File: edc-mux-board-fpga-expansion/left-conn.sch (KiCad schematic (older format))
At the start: 68 parts

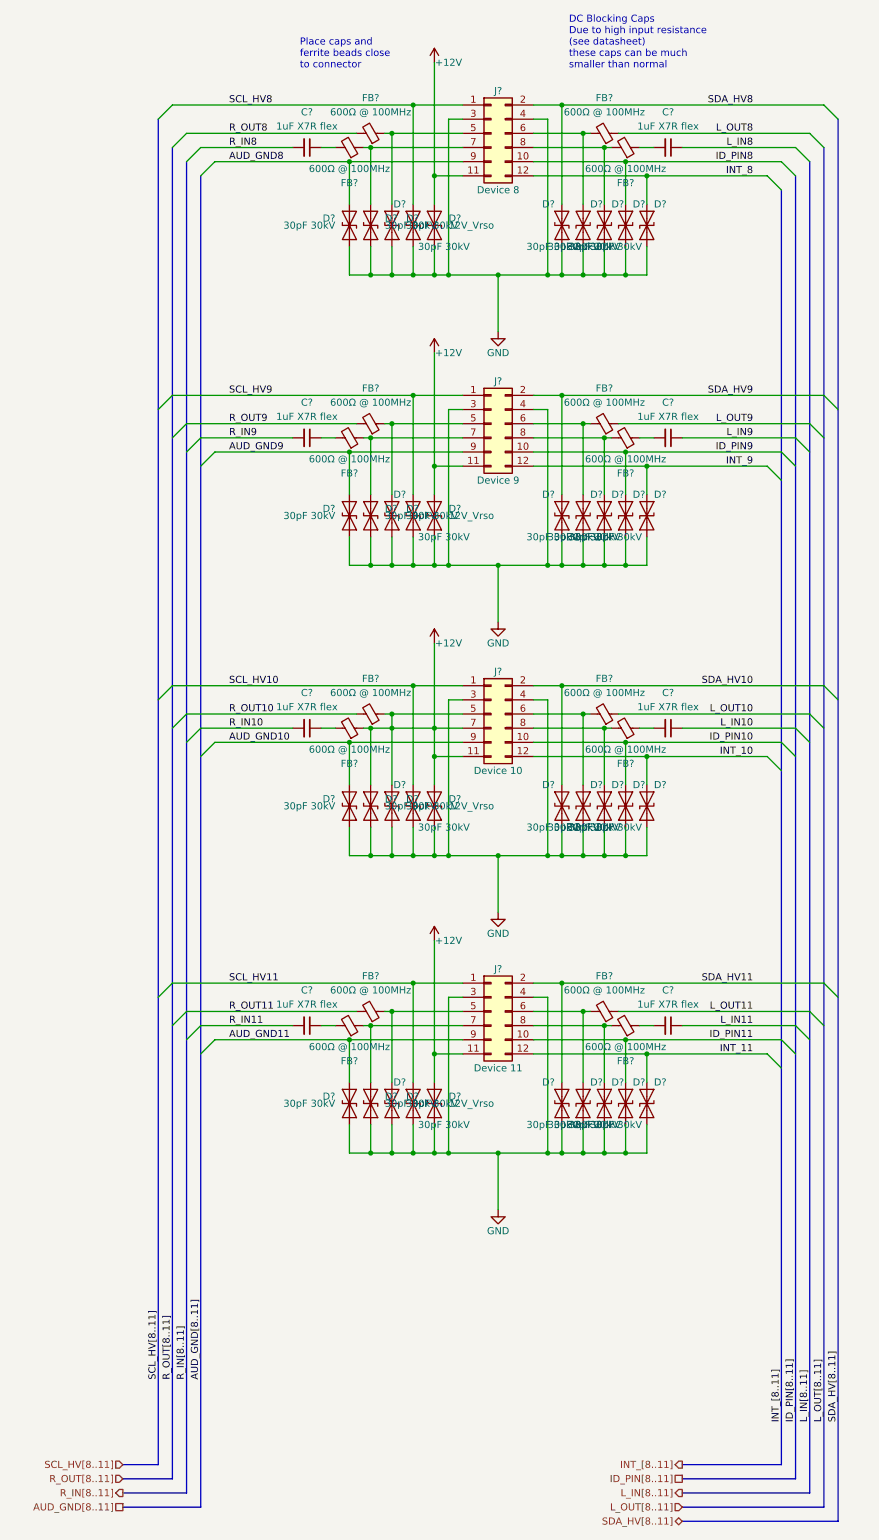
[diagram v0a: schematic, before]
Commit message: Annotating modified components
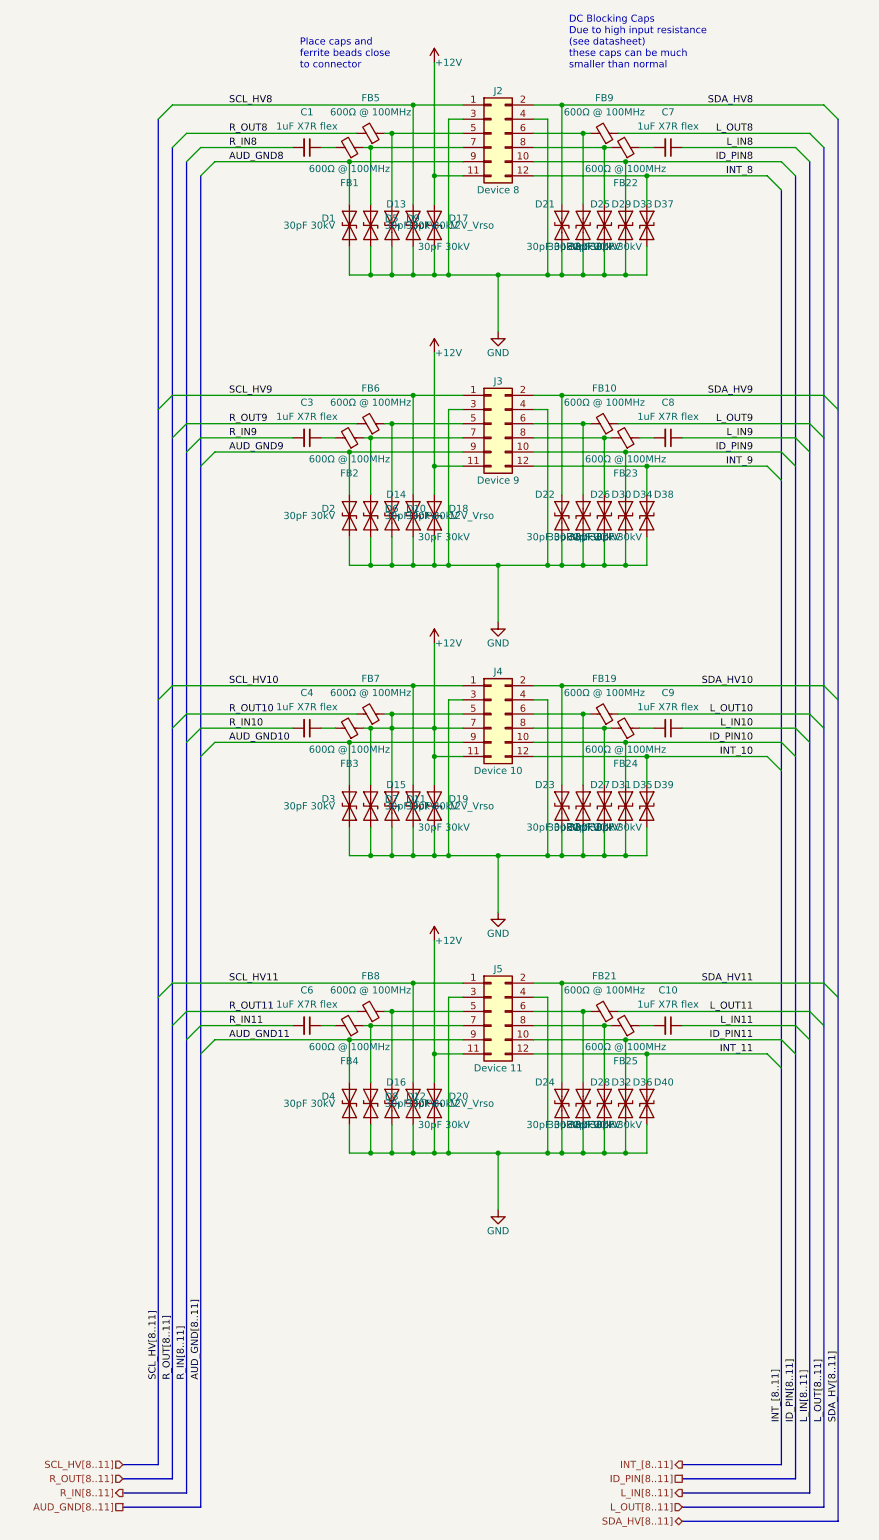
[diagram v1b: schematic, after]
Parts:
- gave numbers to parts that had none: 68

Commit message: Reannotating entire schematic
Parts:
- renumbered C1 to C154, C3 to C155, C4 to C156, C6 to C157, C7 to C158, C8 to C159, C9 to C160, C10 to C161, FB1 to FB10, FB2 to FB11, FB3 to FB12, FB4 to FB13, FB5 to FB14, FB6 to FB15, FB7 to FB16, FB8 to FB17, FB9 to FB18, FB10 to FB19, FB19 to FB20
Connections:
- net +12V: no longer D11.1 (A1), D7.1 (A1), FB12.1, FB16.1, J4.5 (Pin_5), J4.7 (Pin_7)
- new net: D11.1 (A1), FB16.1, J4.5 (Pin_5)
- new net: D7.1 (A1), FB12.1, J4.7 (Pin_7)

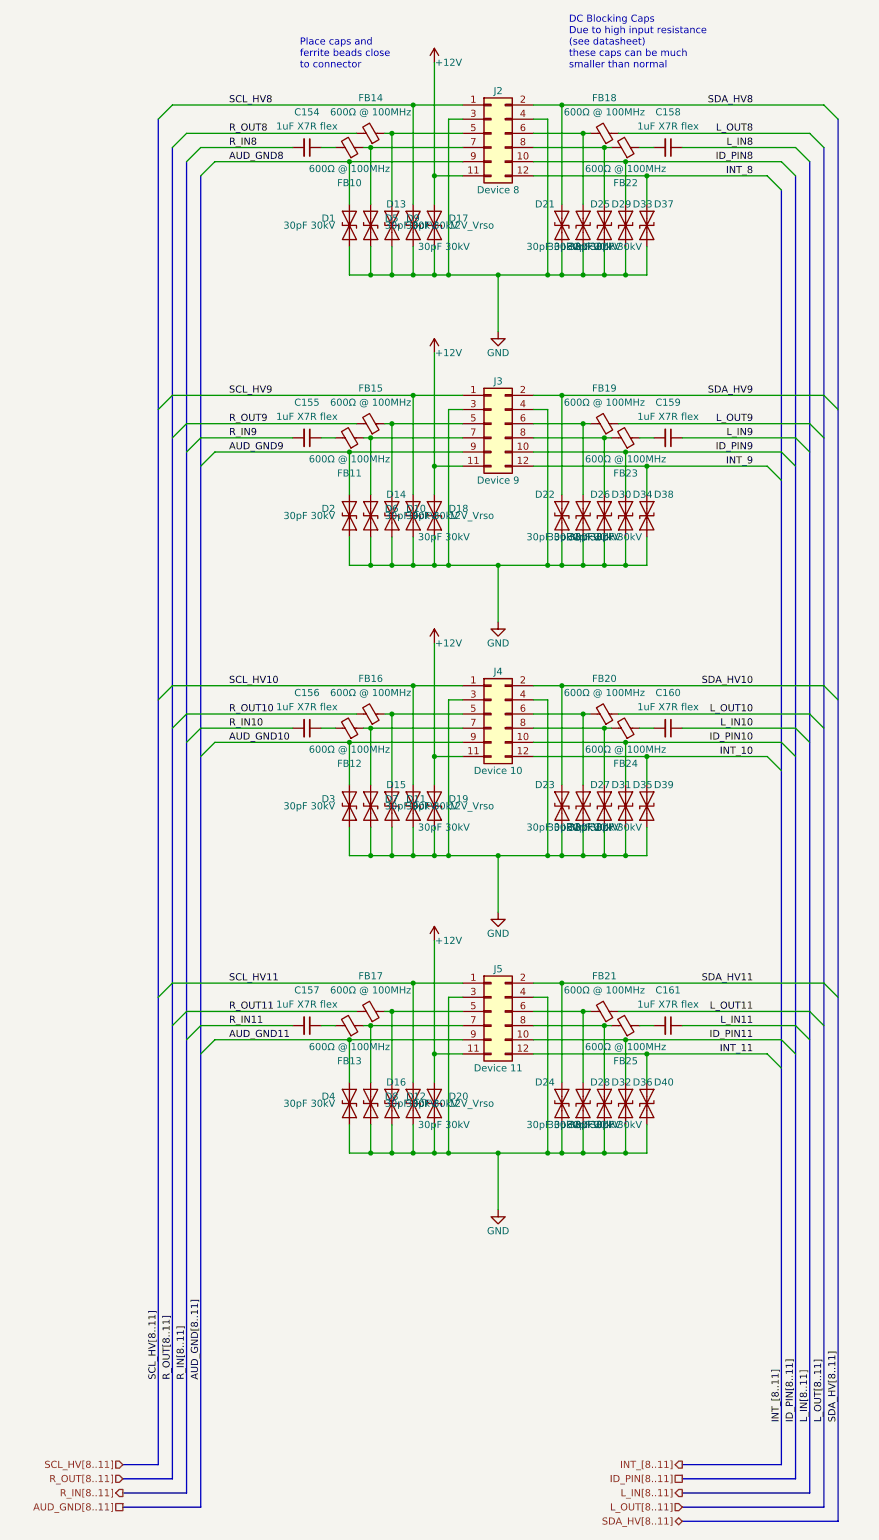
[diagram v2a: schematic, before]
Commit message: Revert "Reannotating entire schematic"
This reverts commit 97c3612cc2b740b2bdf3282f0b448b6cc86bc5bb.
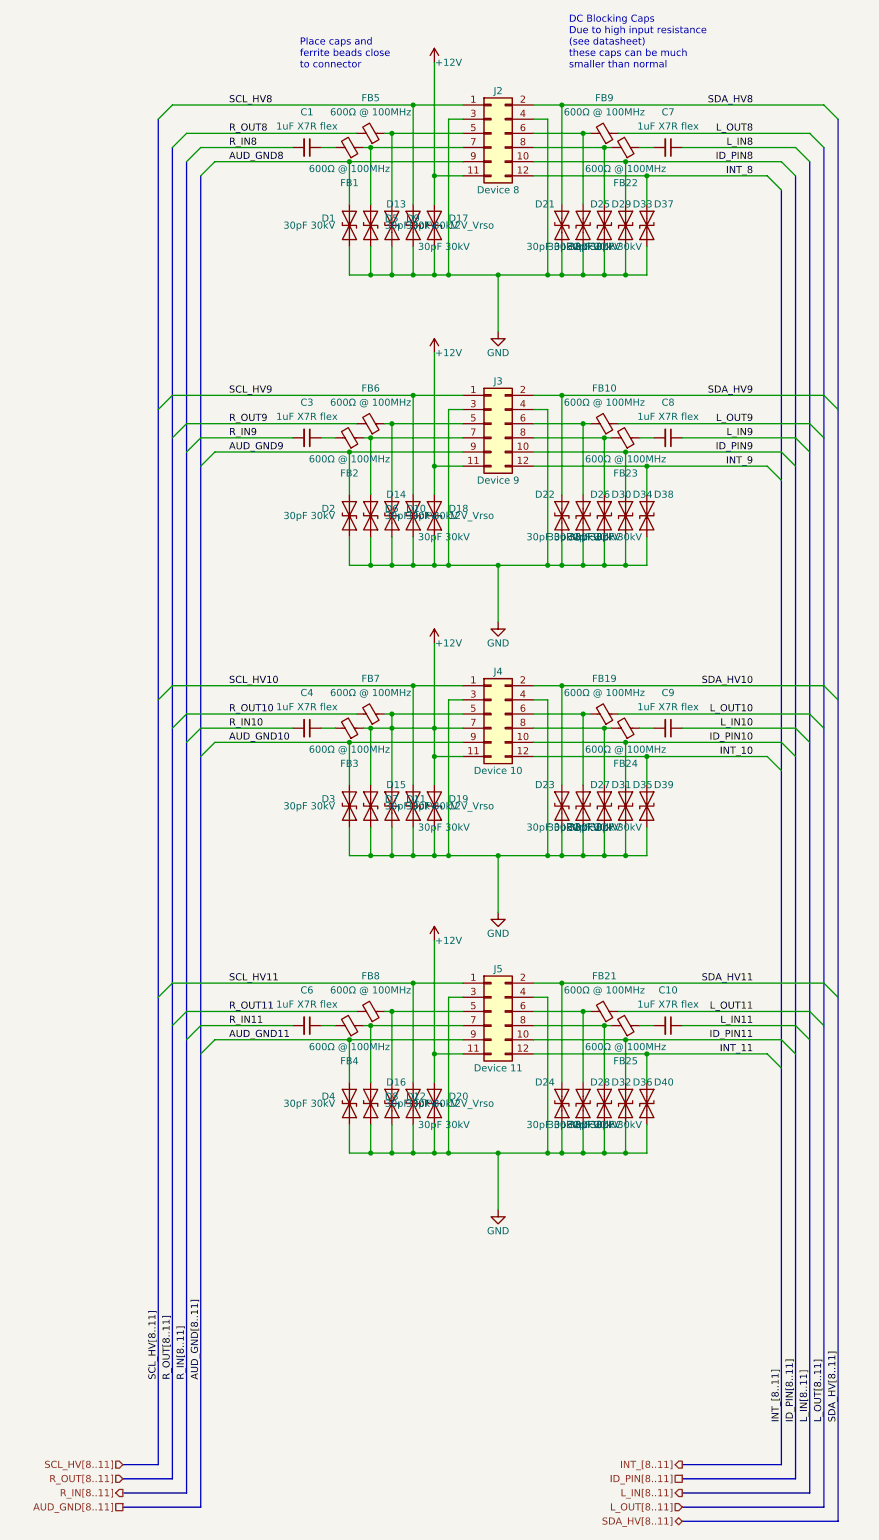
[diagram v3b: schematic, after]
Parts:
- renumbered C154 to C1, C161 to C10, C155 to C3, C156 to C4, C157 to C6, C158 to C7, C159 to C8, C160 to C9, FB10 to FB1, FB19 to FB10, FB20 to FB19, FB11 to FB2, FB12 to FB3, FB13 to FB4, FB14 to FB5, FB15 to FB6, FB16 to FB7, FB17 to FB8, FB18 to FB9
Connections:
- net +12V: now also D11.1 (A1), D7.1 (A1), FB3.1, FB7.1, J4.5 (Pin_5), J4.7 (Pin_7)

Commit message: Figured out what option to use to reannotate the schematic properly
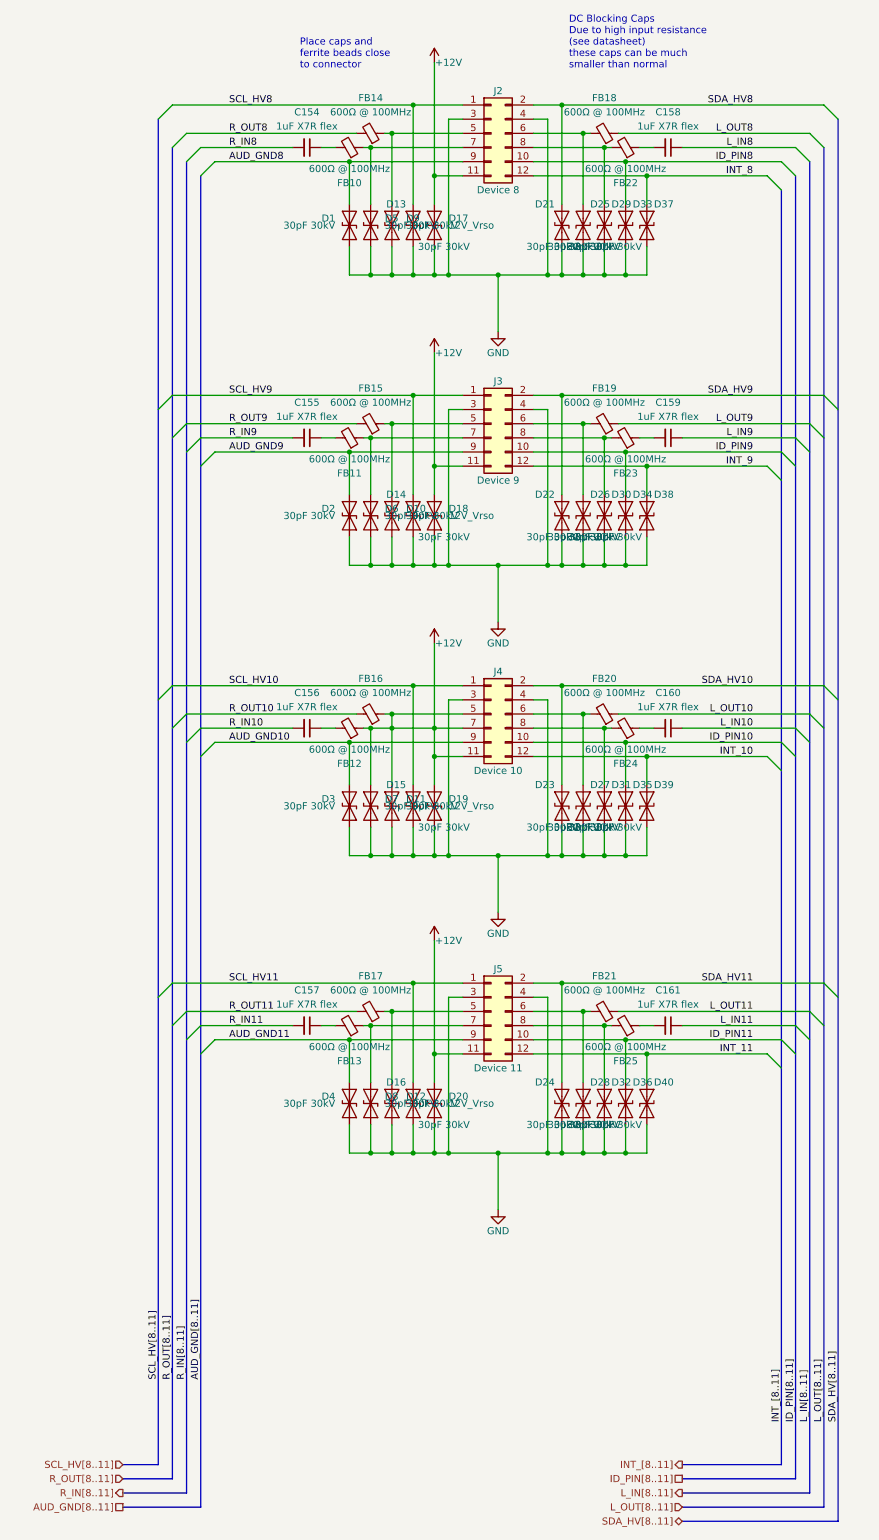
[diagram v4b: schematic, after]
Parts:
- renumbered C1 to C154, C3 to C155, C4 to C156, C6 to C157, C7 to C158, C8 to C159, C9 to C160, C10 to C161, FB1 to FB10, FB2 to FB11, FB3 to FB12, FB4 to FB13, FB5 to FB14, FB6 to FB15, FB7 to FB16, FB8 to FB17, FB9 to FB18, FB10 to FB19, FB19 to FB20

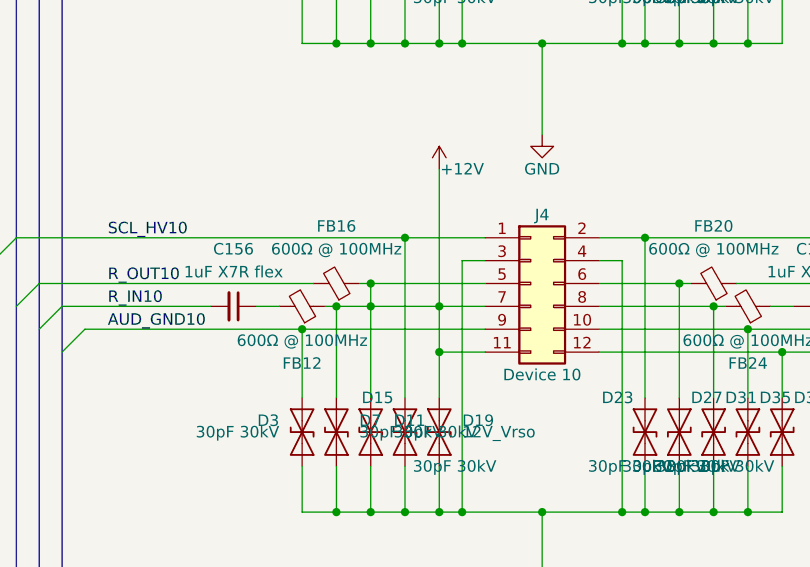
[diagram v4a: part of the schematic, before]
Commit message: removed extra connections
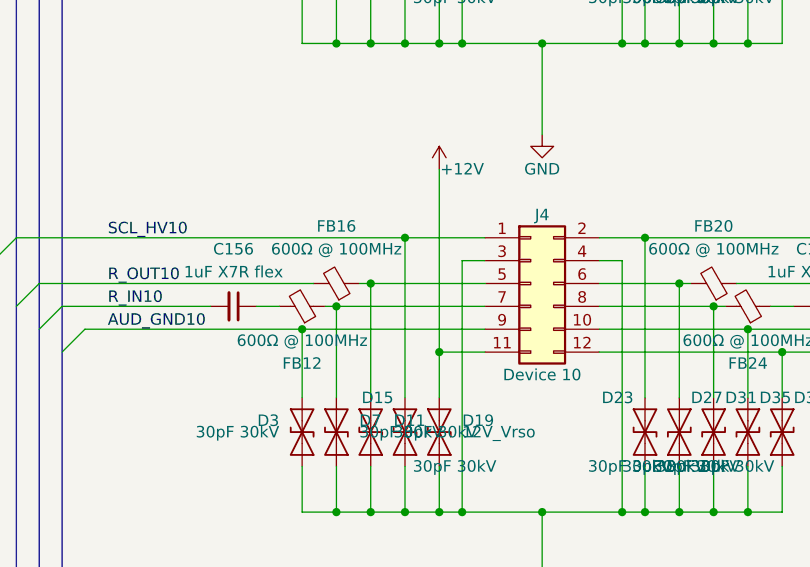
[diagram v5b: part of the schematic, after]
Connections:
- net +12V: no longer D11.1 (A1), D7.1 (A1), FB12.1, FB16.1, J4.5 (Pin_5), J4.7 (Pin_7)
- new net: D11.1 (A1), FB16.1, J4.5 (Pin_5)
- new net: D7.1 (A1), FB12.1, J4.7 (Pin_7)
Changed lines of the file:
@@
 	4100 6400 3900 6400
-Wire Wire Line
-	3900 6400 3900 6200
 Wire Wire Line
 	4600 6400 5400 6400
@@
 	0    1    1    0
 $EndComp
-Wire Wire Line
-	3600 6100 3600 6200
 Connection ~ 3600 6100
 Wire Wire Line
@@
 Wire Bus Line
 	6750 11800 5650 11800
-Connection ~ 3600 6200
-Wire Wire Line
-	3600 6200 3600 6600
 Wire Wire Line
 	3600 6200 3900 6200
-Connection ~ 3900 6200
-Wire Wire Line
-	3900 6200 3900 5600
 Wire Wire Line
 	3900 6200 4100 6200
 Wire Bus Line
 	6750 1900 6750 11800
+Wire Wire Line
+	3600 6100 3600 6600
+Wire Wire Line
+	3900 5600 3900 6400
 Wire Bus Line
 	1950 1900 1950 11400
@@
 	2050 2100 2050 11500
 Wire Bus Line
+	6450 2300 6450 11500
+Wire Bus Line
+	6550 2200 6550 11600
+Wire Bus Line
+	6650 2100 6650 11700
+Wire Bus Line
 	6350 2400 6350 11400
-Wire Bus Line
-	6450 2300 6450 11500
-Wire Bus Line
-	6550 2200 6550 11600
-Wire Bus Line
-	6650 2100 6650 11700
 $EndSCHEMATC
